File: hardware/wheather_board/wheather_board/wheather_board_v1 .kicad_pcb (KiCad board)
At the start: 2 copper layers, 115 x 80 mm, 67 parts, among them J1 Conn_01x02_Female, J10 Conn_01x05_Female, J2 Conn_01x02_Male, J4 Conn_01x03_Male, J5 Conn_01x06_Male, J6 Conn_01x05_Female, J7 Conn_01x06_Female, J8 Conn_01x04_Male, J9 Conn_Coaxial, SW1 SW_MEC_5G, U1 LD1117S50TR_SOT223, U2 BME680, U3 ADS1232IPW, U4 LD39050PUR, U5 REF5050AD, U6 LoRa-E5, U7 CRE1S0505SC

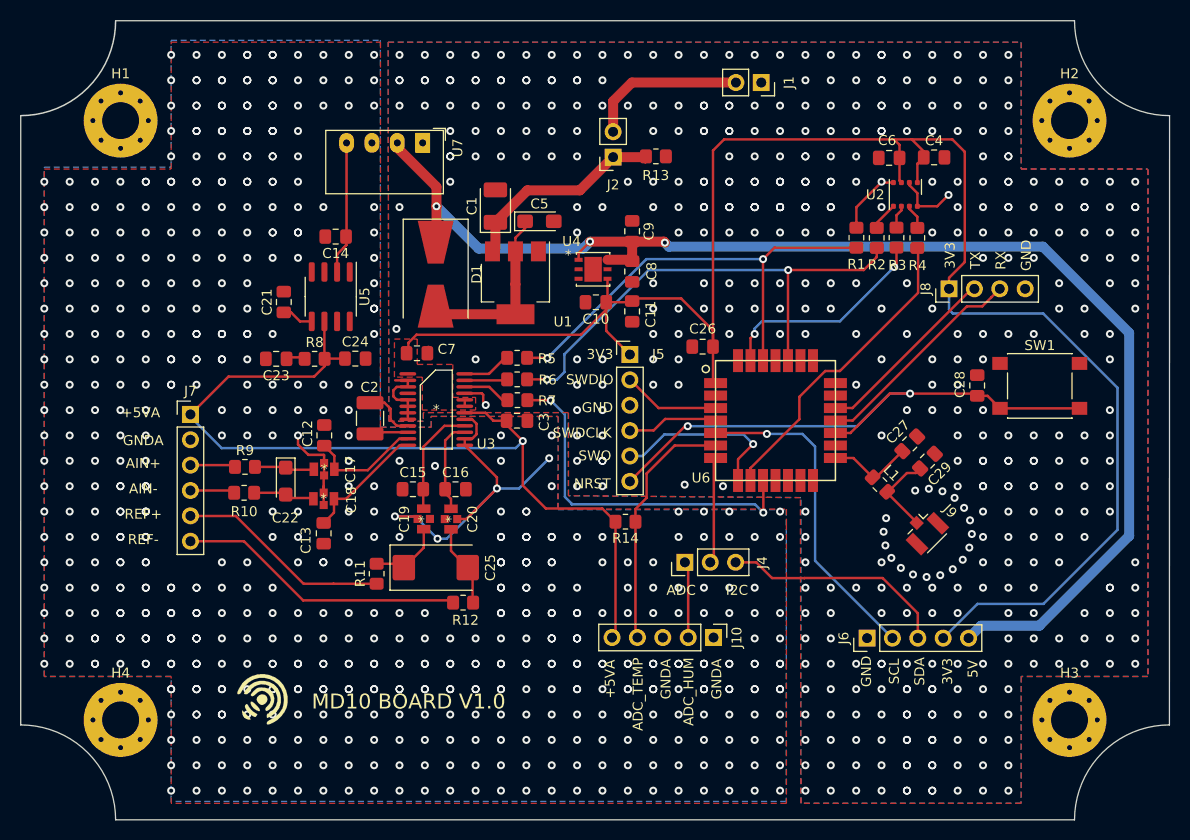
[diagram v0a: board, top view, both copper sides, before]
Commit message: fix some hardware bugs and add an optocoupler
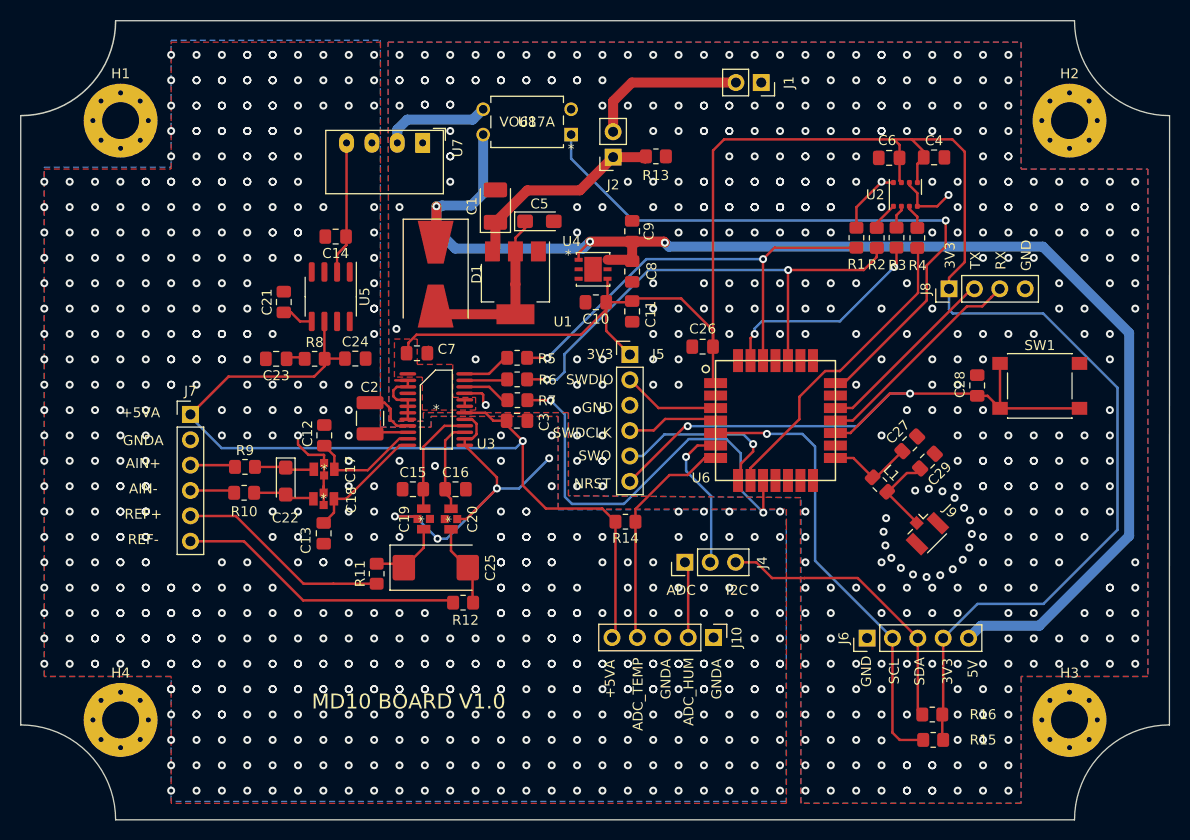
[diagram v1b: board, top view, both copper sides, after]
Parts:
- removed G***: MELLIA, Symbol:logo_mellia
- added R15: R, Resistor_SMD:R_0805_2012Metric_Pad1.20x1.40mm_HandSolder, F.Cu at (175.3, 127.0)
- added R16: R, Resistor_SMD:R_0805_2012Metric_Pad1.20x1.40mm_HandSolder, F.Cu at (175.3, 124.5)
- added U8: VO617A, footprints:VO617A, F.Cu at (139.1, 66.4)
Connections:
- C17 pad 4: GNDA -> (no net)
- C18 pad 4: GNDA -> (no net)
- J6 pad 4: +3V3 -> +3.3V
- SW1 pad 1: GND -> /NRST
- U3 pad 4: Net-(U3-Pad4) -> unconnected-(U3-Pad4)
- U4 pad 3: Net-(U4-Pad3) -> unconnected-(U4-Pad3)
- U4 pad 5: Net-(U4-Pad5) -> unconnected-(U4-Pad5)
- U5 pad 1: Net-(U5-Pad1) -> unconnected-(U5-Pad1)
- U5 pad 3: Net-(U5-Pad3) -> unconnected-(U5-Pad3)
- U5 pad 7: Net-(U5-Pad7) -> unconnected-(U5-Pad7)
- U5 pad 8: Net-(U5-Pad8) -> unconnected-(U5-Pad8)
- U6 pad 11: Net-(U6-Pad11) -> unconnected-(U6-Pad11)
- U6 pad 12: Net-(U6-Pad12) -> unconnected-(U6-Pad12)
- U6 pad 13: Net-(U6-Pad13) -> unconnected-(U6-Pad13)
- U6 pad 20: Net-(U6-Pad20) -> unconnected-(U6-Pad20)
- U6 pad 21: Net-(U6-Pad21) -> /EN_VDDA
- U6 pad 23: Net-(U6-Pad23) -> unconnected-(U6-Pad23)
- U6 pad 25: Net-(U6-Pad25) -> unconnected-(U6-Pad25)
- U6 pad 28: Net-(U6-Pad28) -> unconnected-(U6-Pad28)
- U6 pad 6: /ADC_TEMP -> Net-(J4-Pad2)
- U6 pad 7: Net-(J4-Pad2) -> /ADC_TEMP
- U7 pad 2: +5V -> Net-(U7-Pad2)
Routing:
- net /EN_VDDA: track 0.00 -> 63.8 mm, vias 0 -> 1
- net /I2C_SCL: track 32.9 -> 45.7 mm
- net Net-(U7-Pad2): track 0.00 -> 11.3 mm
- net +3.3V: track 0.00 -> 10.3 mm
- net /ADS_NSS: track 36.4 -> 43.9 mm
- net /I2C_SDA: track 22.8 -> 29.2 mm
- net Net-(J4-Pad2): track 10.7 -> 15.6 mm, vias 0 -> 1
- net +5V: track 135.4 -> 139.9 mm
- net /NRST: track 58.4 -> 62.9 mm
- net /ADC_TEMP: track 25.2 -> 23.5 mm
- net GND: track 18.7 -> 19.0 mm, vias 452 -> 425
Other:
- net class Default removed
